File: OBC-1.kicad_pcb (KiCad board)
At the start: 6 copper layers, 42.8 x 42.8 mm, 112 parts, among them J1 ERM8-020-X, J2 ERF6-020-X, J3 Conn_01x02_Female, Q1 MGSF1N02L, Q2 MGSF1N02L, U1 TPS62850x-Q1, U11 TMS5701227CZWTQQ1, U2 TPS62850x-Q1, U3 LTC4353, U4 SN65HVD230M-EP, U5 SN65HVD230M-EP, U6 SN65HVD230M-EP

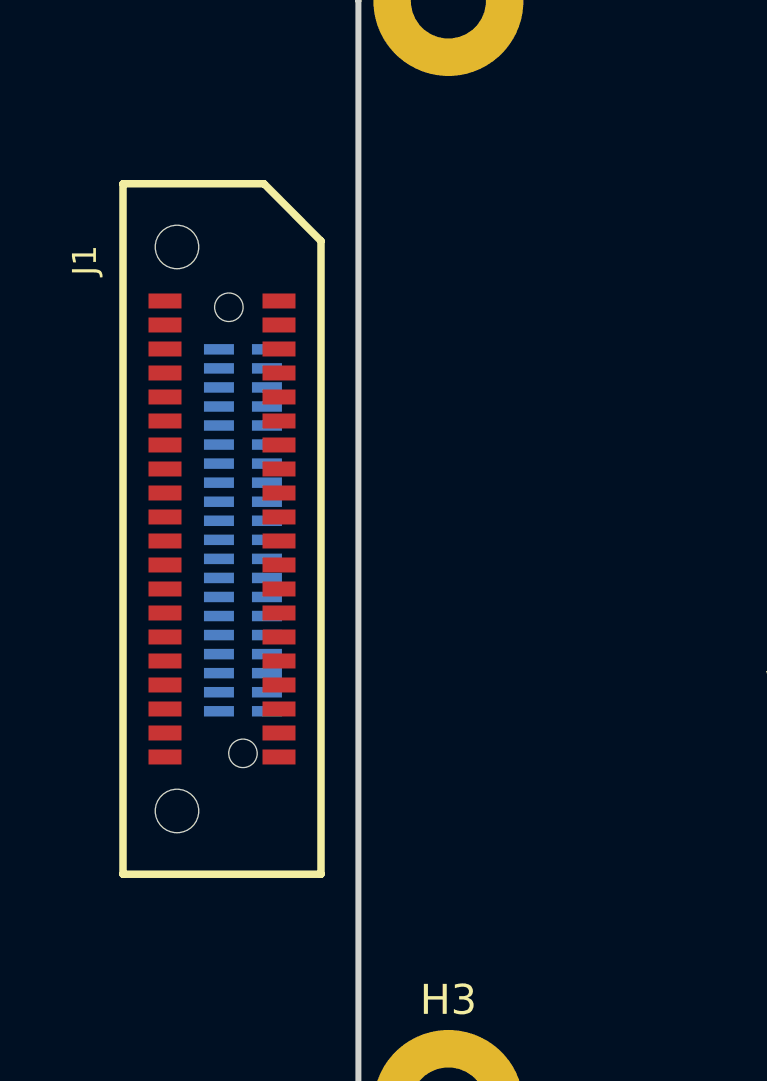
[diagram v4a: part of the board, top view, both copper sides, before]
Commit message: finalised connector position, updated testpoint footprint assingment. SMPS footprint netlist has a bug that will hopefully be fixed when it has a valid footprint
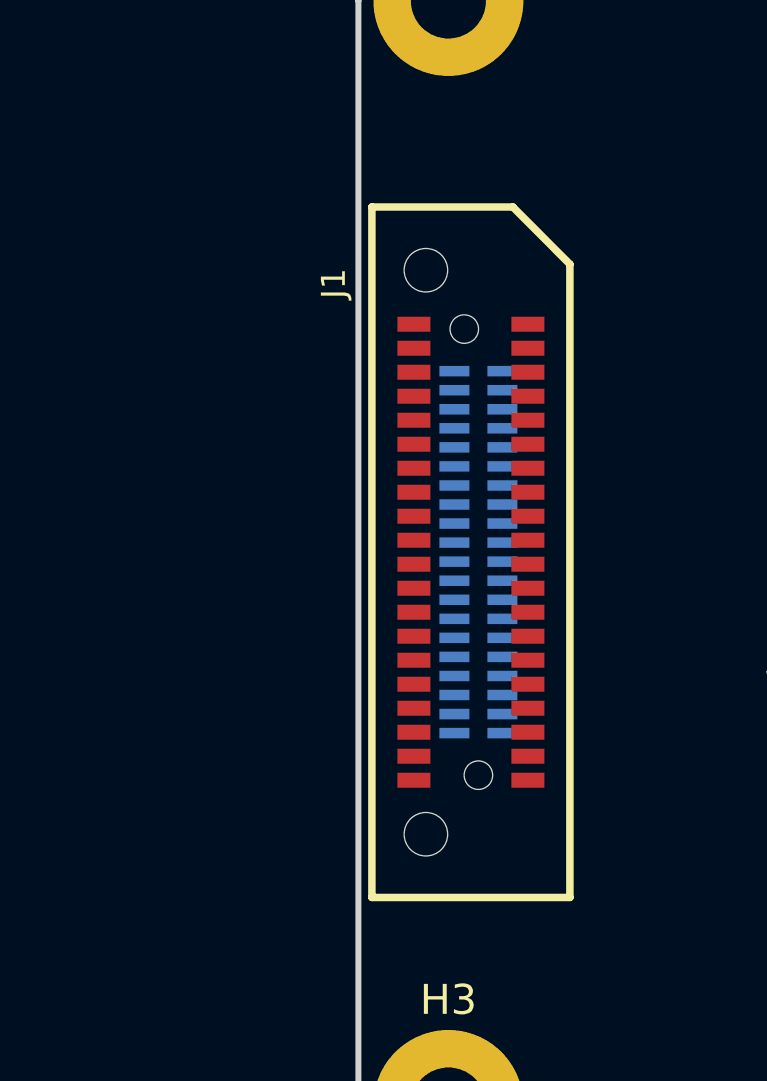
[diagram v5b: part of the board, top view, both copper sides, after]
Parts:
- J3: footprint TFT_TestPoints:TestPoint_2Pads_Pitch2.54mm_Drill0.8mm -> TFT_TestPoints:TP_2Pads_Pitch2.54mm_Drill0.8mm
- TP1, TP10, TP11, TP12, TP13, TP14, TP15, TP16, TP17, TP18, TP19, TP2, TP20, TP21, TP22, TP23, TP24, TP25, TP26, TP27, TP28, TP29, TP3, TP4, TP5, TP6, TP7, TP8, TP9: footprint TFT_TestPoints:TestPoint_Pad_D1.0mm -> TFT_TestPoints:TP_RDPad_D1.0mm
- moved J1 8.33 mm to (92.7, 92.9)
- moved J2 7.88 mm to (92.9, 92.9)
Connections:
- TP1 pad 1: (no net) -> /TMS570_uC/JTAG_RTCK
- TP10 pad 1: (no net) -> GND
- TP11 pad 1: (no net) -> GND
- TP12 pad 1: (no net) -> GND
- TP13 pad 1: (no net) -> GND
- TP14 pad 1: (no net) -> GND
- TP15 pad 1: (no net) -> GND
- TP16 pad 1: (no net) -> Net-(C4-Pad2)
- TP17 pad 1: (no net) -> OBC_1V25_P
- TP18 pad 1: (no net) -> OBC_1V2_R
- TP19 pad 1: (no net) -> OBC_1V25
- TP2 pad 1: (no net) -> /TMS570_uC/JTAG_TDI
- TP20 pad 1: (no net) -> /CAN_XCVR_R/CAN_PL_R
- TP21 pad 1: (no net) -> /CAN_XCVR_R/CAN_PL_D
- TP22 pad 1: (no net) -> /CAN_XCVR_PL/CAN_PL_D
- TP23 pad 1: (no net) -> /TMS570_uC/CAN_PA_R
- TP24 pad 1: (no net) -> /CAN_XCVR_PL/CAN_PL_R
- TP25 pad 1: (no net) -> /TMS570_uC/CAN_PA_D
- TP26 pad 1: (no net) -> OBC_3V3
- TP27 pad 1: (no net) -> /Supervisor_RTC_FRAM/SPVSR_nRST
- TP28 pad 1: (no net) -> /TMS570_uC/OBC_I2C_SDA
- TP29 pad 1: (no net) -> /TMS570_uC/OBC_I2C_SCL
- TP3 pad 1: (no net) -> /TMS570_uC/JTAG_TEST
- TP4 pad 1: (no net) -> /TMS570_uC/JTAG_nTRST
- TP5 pad 1: (no net) -> /TMS570_uC/JTAG_TCK
- TP6 pad 1: (no net) -> /TMS570_uC/JTAG_TDO
- TP7 pad 1: (no net) -> /TMS570_uC/JTAG_TMS
- TP8 pad 1: (no net) -> GND
- TP9 pad 1: (no net) -> GND
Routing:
- added copper zone on In3.Cu, net OBC_1V25
- removed copper zone on In3.Cu, net OBC_1V2

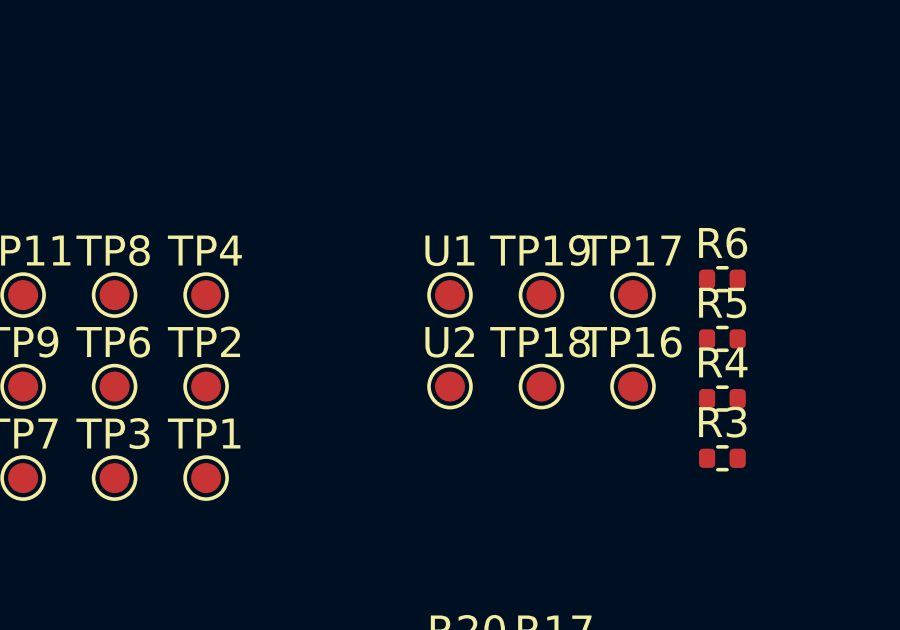
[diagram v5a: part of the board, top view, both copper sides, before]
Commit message: fixed incorrect footprint assignment to U1 and U2
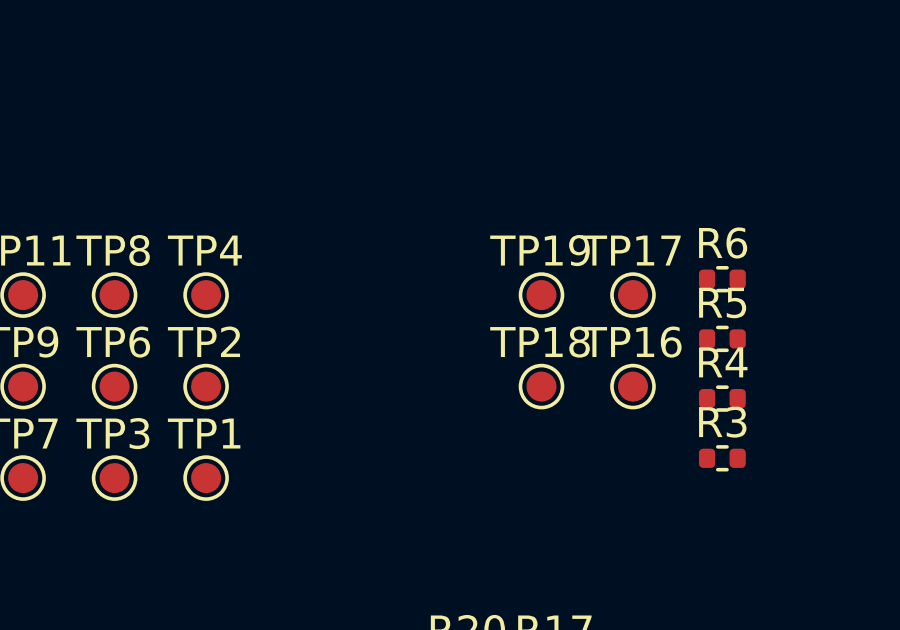
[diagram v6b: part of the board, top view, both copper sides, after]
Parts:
- removed U1, U2: TPS62850x-Q1, TFT_TestPoints:TestPoint_Pad_D1.0mm

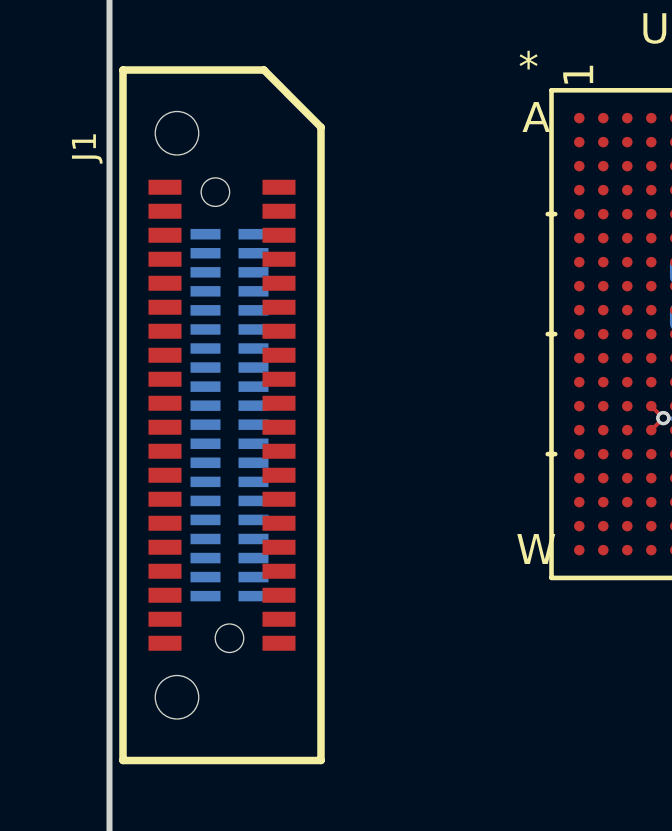
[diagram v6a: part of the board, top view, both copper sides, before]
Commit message: connectors broken out
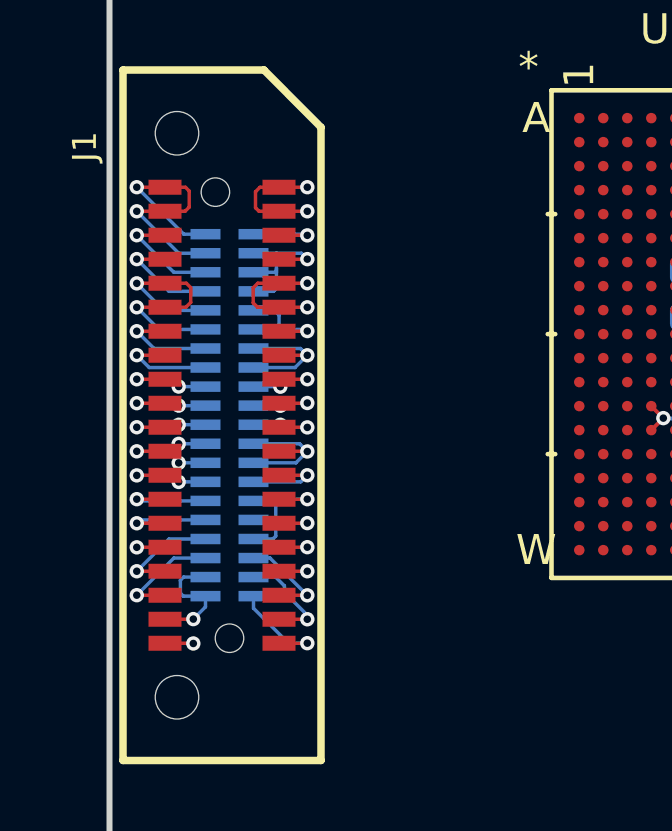
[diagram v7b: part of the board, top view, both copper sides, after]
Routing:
- net GND: track 39.1 -> 108.7 mm, vias 12 -> 39
- net PAYLOAD_5V: track 0.00 -> 9.95 mm, vias 0 -> 2
- net PAYLOAD_3V3: track 0.00 -> 9.48 mm, vias 0 -> 2
- net OBC_5V: track 0.00 -> 4.23 mm, vias 0 -> 2
- net OBC_3V3: track 26.0 -> 30.1 mm, vias 12 -> 14
- net /Connectors/CAN_H_PA: track 0.00 -> 3.75 mm, vias 0 -> 1
- net /Connectors/CAN_L_PA: track 0.00 -> 3.68 mm, vias 0 -> 1
- net /CAN_XCVR_R/CAN_L_PL: track 0.00 -> 3.62 mm, vias 0 -> 1
- net /CAN_XCVR_R/CAN_H_PL: track 0.00 -> 3.53 mm, vias 0 -> 1
- net /TMS570_uC/OBC_I2C_SCL: track 0.00 -> 0.95 mm, vias 0 -> 1
- net /CAN_XCVR_PL/CAN_H_PL: track 0.00 -> 0.95 mm, vias 0 -> 1
- net /Connectors/ADS_nRST: track 0.00 -> 0.95 mm, vias 0 -> 1
- net /CAN_XCVR_PL/CAN_L_PL: track 0.00 -> 0.95 mm, vias 0 -> 1
- net /TMS570_uC/OBC_I2C_SDA: track 0.00 -> 0.94 mm, vias 0 -> 1
- net /Connectors/GPS_STS: track 0.00 -> 0.94 mm, vias 0 -> 1
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
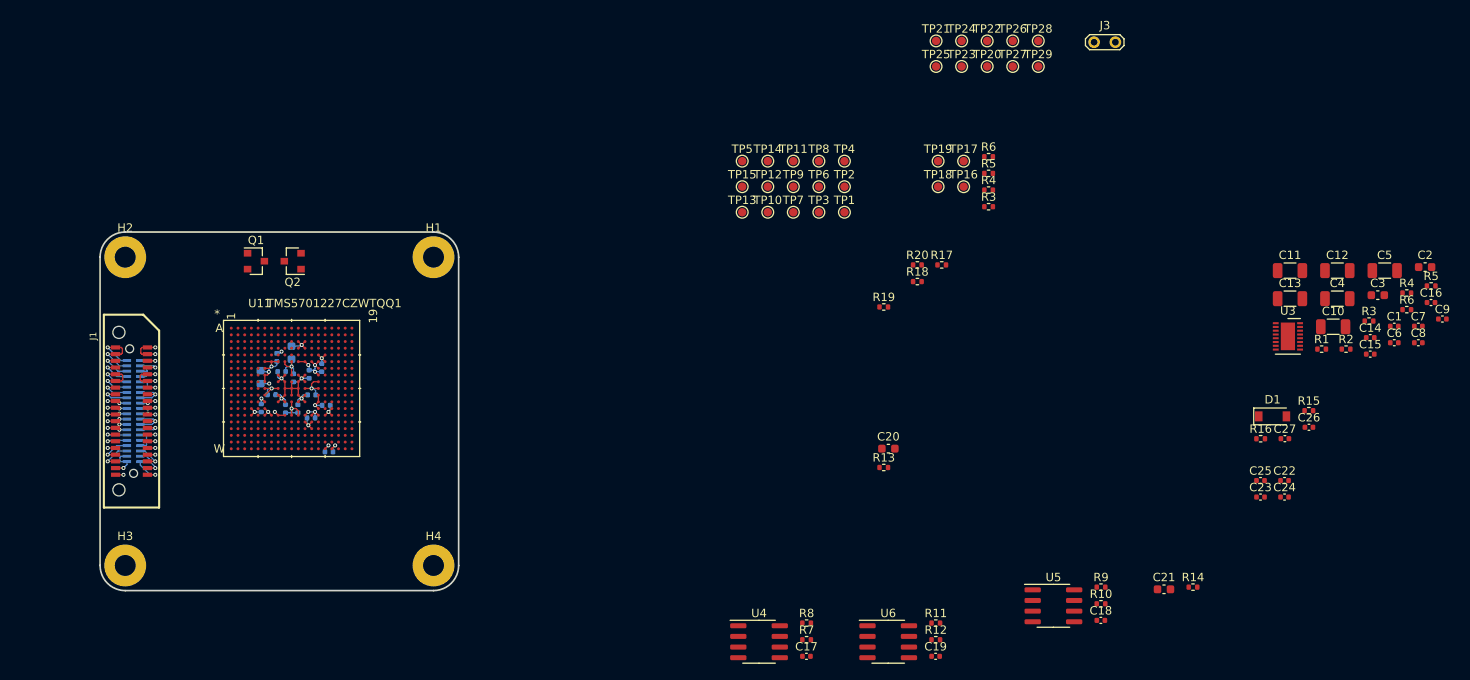
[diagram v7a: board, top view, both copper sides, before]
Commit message: updates to CAN power trace routing and initial CAN differential rail routing
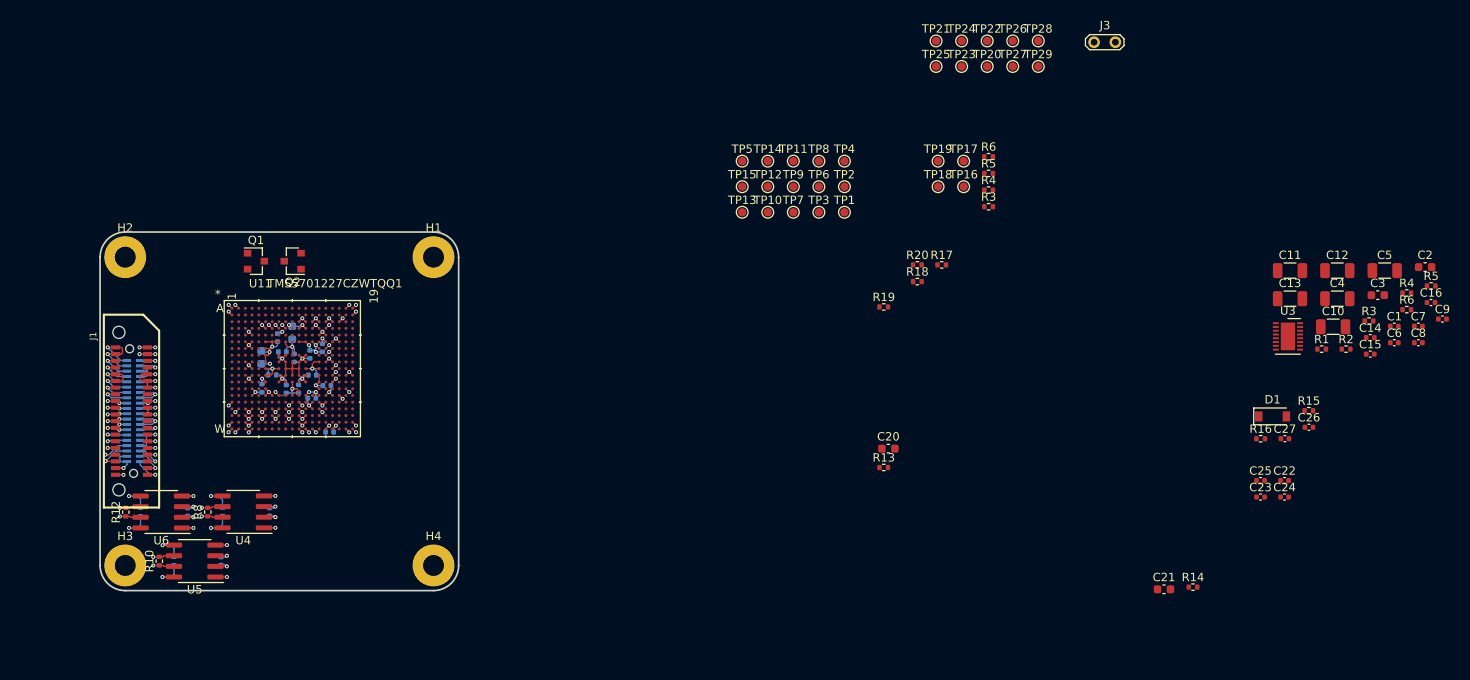
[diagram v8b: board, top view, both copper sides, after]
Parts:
- C17, C18, C19, R11, R7, R9: moved to B.Cu
- moved R10 112.5 mm to (96.0, 110.8), turned to 90 degrees
- moved R9 110.7 mm to (97.7, 110.8), turned to 270 degrees
- moved C18 105.3 mm to (103.3, 110.8), turned to 270 degrees
- moved U5 102.6 mm to (100.2, 110.8), turned to 180 degrees
- moved R12 97.9 mm to (92.0, 104.9), turned to 90 degrees
- moved R11 95.8 mm to (93.7, 104.9), turned to 270 degrees
- moved C19 90.9 mm to (99.3, 104.9), turned to 270 degrees
- moved U6 88.1 mm to (96.2, 104.9), turned to 180 degrees
- moved R8 72.7 mm to (101.8, 104.9), turned to 90 degrees
- moved R7 71.4 mm to (103.5, 104.9), turned to 270 degrees
- moved C17 66.4 mm to (109.1, 104.9), turned to 270 degrees
- moved U4 63.5 mm to (106.0, 104.9), turned to 180 degrees
- moved C28 2.37 mm to (108.1, 86.5)
- moved C32 2.37 mm to (112.1, 86.5)
- moved C33 2.37 mm to (111.1, 90.2)
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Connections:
- J1 pad 15: /CAN_XCVR_PL/CAN_H_PL -> /CAN_XCVR_PL/CAN_L_PL
- J1 pad 16: /CAN_XCVR_PL/CAN_L_PL -> /CAN_XCVR_PL/CAN_H_PL
- J1 pad 19: /CAN_XCVR_R/CAN_H_PL -> /CAN_XCVR_R/CAN_L_PL
- J1 pad 20: /CAN_XCVR_R/CAN_L_PL -> /CAN_XCVR_R/CAN_H_PL
- J2 pad 19: /CAN_XCVR_R/CAN_H_PL -> /CAN_XCVR_R/CAN_L_PL
- J2 pad 20: /CAN_XCVR_R/CAN_L_PL -> /CAN_XCVR_R/CAN_H_PL
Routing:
- net GND: track 108.7 -> 159.3 mm, vias 39 -> 102
- net /CAN_XCVR_R/CAN_H_PL: track 3.53 -> 17.6 mm, vias 1 -> 2
- net /CAN_XCVR_R/CAN_L_PL: track 3.62 -> 17.3 mm, vias 1 -> 2
- net /CAN_XCVR_PL/CAN_H_PL: track 0.95 -> 14.2 mm, vias 1 -> 2
- net /CAN_XCVR_PL/CAN_L_PL: track 0.95 -> 13.7 mm, vias 1 -> 2
- net OBC_3V3: track 30.1 -> 40.9 mm, vias 14 -> 19
- net /Connectors/CAN_H_PA: track 3.75 -> 14.1 mm, vias 1 -> 2
- net /Connectors/CAN_L_PA: track 3.68 -> 13.8 mm, vias 1 -> 2
- net Net-(R9-Pad2): track 0.00 -> 3.93 mm, vias 0 -> 1
- net Net-(R7-Pad2): track 0.00 -> 3.92 mm, vias 0 -> 1
- net Net-(R11-Pad2): track 0.00 -> 3.91 mm, vias 0 -> 1
- net /TMS570_uC/CAN_PA_Rs: track 0.00 -> 2.55 mm, vias 0 -> 1
- net /CAN_XCVR_R/CAN_PL_Rs: track 0.00 -> 2.53 mm, vias 0 -> 1
- net /CAN_XCVR_PL/CAN_PL_Rs: track 0.00 -> 2.49 mm, vias 0 -> 1
- net /CAN_XCVR_PL/CAN_PL_D: track 0.00 -> 1.37 mm, vias 0 -> 1
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- added copper zone on In2.Cu, net OBC_3V3
